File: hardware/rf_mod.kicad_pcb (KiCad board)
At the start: 4 copper layers, 100 x 100 mm, 168 parts, among them J1001 SMA, J1002 SMA, J1003 SMA, J1004 Pmod, J101 SMA, J102 SMA, J103 SMA, J1201 SMA, J1202 SMA, J1301 SMA, J1302 SMA, J1303 SMA, J201 SMA, J202 SMA, J401 SMA, J402 SMA, J501 SMA, J502 SMA, J701 SMA, J702 SMA, J703 SMA, J801 SMA, J802 SMA, J803 SMA, J901 USB-C, J902 SMA, Q1001 AO3401A, Q1201 AO3401A, Q1301 AO3401A, Q501 AO3401A, Q701 AO3401A, Q801 AO3401A, SW1001 ON, SW1201 ON, SW1301 ON, SW501 ON, SW701 ON, SW801 ON, U1001 3.3V, U1002 MAX2871, U101 ADEX-10L+, U1201 GALI-84+, U1301 TRF3722, U1302 3.3V, U501 QPL9547, U701 3.3V, U702 ADL5350, U801 3.3V, U802 ADL5350, U901 MT3608, U902 3.3V, U903 74LVC1G17, X901 25 MHz

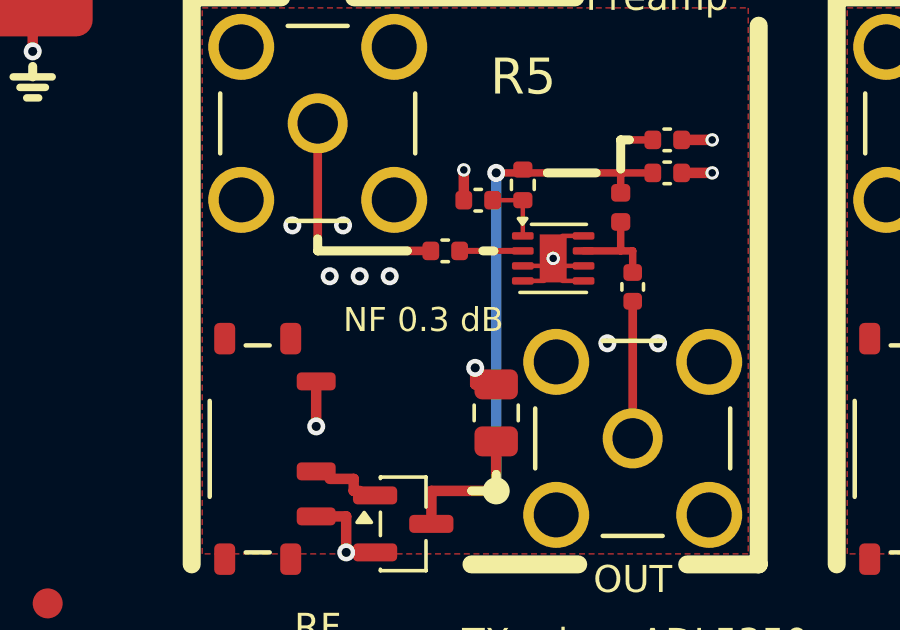
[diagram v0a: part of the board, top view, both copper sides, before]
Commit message: Back-side panels on all six boards; P22 set by hand or by the FPGA; P15 dropped
Jason, Prompt 18: "I hope that the silkscreen (including on the back) is appropriately used to document anything that a
user definitely needs to know to use the tiles successfully and without damaging anything.  If there is additional room
on the back, putting plots of expected responses or other relevant parameters would be great."

- gen_pcb.back_panels: under each tile, mirrored on the back silk, its number and title and the lines in its board's
  BACK dict (levels, loads, supplies, cautions), and where there is one its expected response as a small plot
  (BACK_PLOTS, or the ladder tiles' own simulation; scripts/backplots.py for the rest: amplifiers, datasheet tables,
  the open stub, P23's tuning curve, P10's clipping curve).  A panel goes as one block or in two to four parts, each
  below the one before, clear of the back's tracks and vias where it can be; every panel and plot placed, DRC 0.
- Front silk: Y2 says PULSES ONLY, Y10 "start at mV", R5 and X4 their input level (IN -20 dBm) in place of the noise
  figure.
- P22 (PE43711) on two cells with an 8-way DIP switch: way 1 SPI, ways 2-8 the bits (direct parallel mode with LE pulled
  high), 100 k pull-downs; it still needs the Pmod's 3.3 V.  P15 (two Smith-chart loads) dropped for the cell; P23 moved
  to (3,0).

Co-Authored-By: Claude Opus 5.5 <noreply@anthropic.com>
Claude-Session: https://claude.ai/code/session_01RKeoKvFFzjk3cEBLCXXHnB
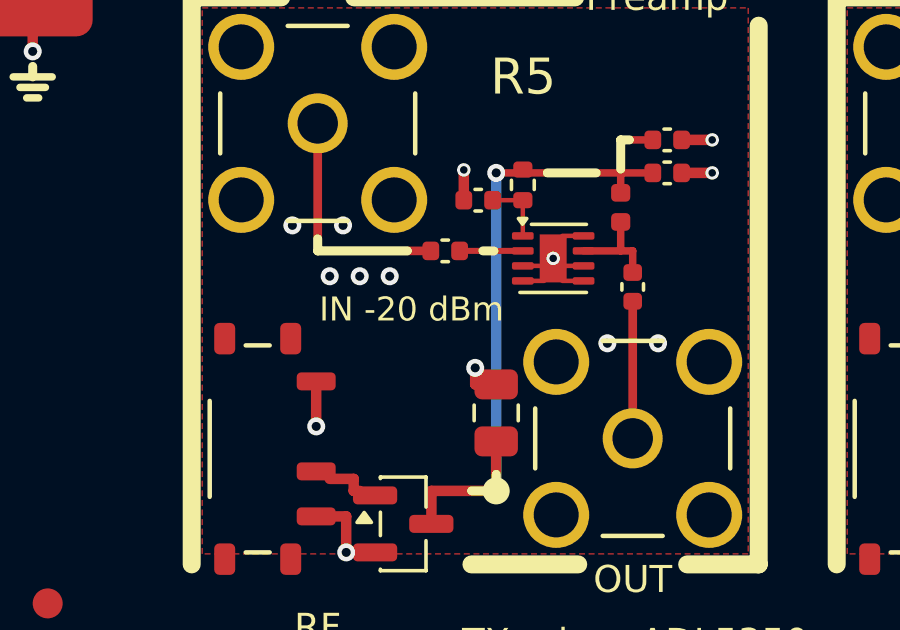
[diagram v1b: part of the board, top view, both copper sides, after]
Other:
- board text added: "+20 dB, OUT"
- board text added: "+22 dBm BURNS"
- board text added: "180 degrees apart"
- board text added: "30 dB pad"
- board text added: "50 ohm"
- board text added: "50 ohm on an unused one"
- board text added: "50 ohm on every port"
- board text added: "I, Q +-1 V into 50 ohm"
- board text added: "IN -20 dBm"
- board text added: "IN < -20 dBm"
- board text added: "IN max +10 dBm"
- board text added: "IN max 0 dBm"
- board text added: "LO 0 to +6 dBm (+4 best)"
- board text added: "OUT A+, A-: -4 to +5 dBm,"
- board text added: "R1 Diode mixer"
- board text added: "R10 Synthesizer"
- board text added: "R12 Gain"
- board text added: "R13 I/Q transmitter"
- board text added: "R2 2.45 GHz filter"
- board text added: "R4 915 MHz filter"
- board text added: "R5 Preamp"
- board text added: "R7 TX mixer ADL5350"
- board text added: "R8 RX mixer ADL5350"
- board text added: "R9 Power"
- board text added: "REF OUT 25 MHz, 1.6 V p-p"
- board text added: "REF: 25 MHz via R10"
- board text added: "RF about -3 dBm"
- board text added: "RF below -5 dBm"
- board text added: "RF, IF max +10 dBm"
- board text added: "USB-C 5 V only"
- board text added: "from a TX"
- board text added: "harmonics below 3 GHz"
- board text added: "image: filter with R2, R4"
- board text added: "into 50 ohm, to R10 REF IN"
- board text added: "max +20 dBm"
- board text added: "slide up: on"
- board text removed: "NF 0.3 dB"

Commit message: One letter per board, tiles in lower case: AMOD-P2 is AMOD-N (n1-n11), RF-MOD-2 is IQ-MOD (q1-q11), PhMOD's tiles h1-h10
Jason, Prompt 19: "If we can have a nice, well justified single-letter designator for each board, it would make
everything much more clear", and "d11, q11, and c11 don't look like obvious electronics or PCB things".

- p passive, n networks (AMOD-P2's P14, P16-P25), a active, r radio, h PhMOD (Y1-Y10), q quadrature (RF-MOD-2's X1-X11);
  c, m and b are taken for the conversion, motor and brushless boards to come.  PLAN.md section 13 has the table and
  the reasons (no letter moves to another board, no retired name is reused, no s: s11 is the reflection coefficient).
- Every tile name in lower case on the silk, in the code (Tile ids, BACK/BACK_PLOTS/DOCS keys, the nets built on them),
  the handbooks, README, DOA lists, KIT, PLAN and the review brief; pin names (USB-C A1...), the 4046's R1/C1, nets
  named N1/P1, part numbers ending -R7 and the paper size A1 left alone.  tiles.dump refuses a tile not named
  <letter><n>, a number twice, and a BACK key for a tile that does not exist.
- Board and file renames: boards/amod_n.py, boards/iq_mod.py, docs/DOA_amod_n.md, docs/DOA_iq_mod.md, the handbooks,
  the generated hardware, outputs and pictures.  Silk nudged where a lower-case p or q hung onto the line below.
- All six boards rebuilt: ERC 0, DRC 0, every check.

Co-Authored-By: Claude Opus 5.5 <noreply@anthropic.com>
Claude-Session: https://claude.ai/code/session_01RKeoKvFFzjk3cEBLCXXHnB
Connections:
- net /R10_AN renamed /r10_AN
- net /R10_AP renamed /r10_AP
- net /R10_BF renamed /r10_BF
- net /R10_CP renamed /r10_CP
- net /R10_G renamed /r10_G
- net /R10_LD renamed /r10_LD
- net /R10_LEDA renamed /r10_LEDA
- net /R10_N2 renamed /r10_N2
- net /R10_NF renamed /r10_NF
- net /R10_OUTA renamed /r10_OUTA
- net /R10_OUTAN renamed /r10_OUTAN
- net /R10_REFI renamed /r10_REFI
- net /R10_REG renamed /r10_REG
- net /R10_RS renamed /r10_RS
- net /R10_TN renamed /r10_TN
- net /R10_V33 renamed /r10_V33
- net /R10_VS renamed /r10_VS
- net /R12_G renamed /r12_G
- net /R12_IN renamed /r12_IN
- net /R12_IN_A renamed /r12_IN_A
- net /R12_OUT renamed /r12_OUT
- net /R12_OUT_A renamed /r12_OUT_A
- net /R12_VD renamed /r12_VD
- net /R12_VS renamed /r12_VS
- net /R13_BBI renamed /r13_BBI
- net /R13_BBQ renamed /r13_BBQ
- net /R13_BIN renamed /r13_BIN
- net /R13_BIP renamed /r13_BIP
- net /R13_BQN renamed /r13_BQN
- net /R13_BQP renamed /r13_BQP
- net /R13_CP renamed /r13_CP
- net /R13_G renamed /r13_G
- net /R13_LD renamed /r13_LD
- net /R13_LEDA renamed /r13_LEDA
- net /R13_N2 renamed /r13_N2
- net /R13_REFI renamed /r13_REFI
- net /R13_RFO renamed /r13_RFO
- net /R13_RFOUT renamed /r13_RFOUT
- net /R13_V33 renamed /r13_V33
- net /R13_VS renamed /r13_VS
- net /R13_VT renamed /r13_VT
- net /R1_IF renamed /r1_IF
- net /R1_LO renamed /r1_LO
- net /R1_RF renamed /r1_RF
- net /R2_IN renamed /r2_IN
- net /R2_OUT renamed /r2_OUT
- net /R4_IN renamed /r4_IN
- net /R4_OUT renamed /r4_OUT
- net /R5_G renamed /r5_G
- net /R5_IN renamed /r5_IN
- net /R5_IN_A renamed /r5_IN_A
- net /R5_OUT renamed /r5_OUT
- net /R5_OUT_A renamed /r5_OUT_A
- net /R5_VB renamed /r5_VB
- net /R5_VS renamed /r5_VS
- net /R7_G renamed /r7_G
- net /R7_IF renamed /r7_IF
- net /R7_IFN renamed /r7_IFN
- net /R7_LOC renamed /r7_LOC
- net /R7_LOJ renamed /r7_LOJ
- net /R7_LON renamed /r7_LON
- net /R7_RFIF renamed /r7_RFIF
- net /R7_RFN renamed /r7_RFN
- net /R7_V33 renamed /r7_V33
- net /R7_VPOS renamed /r7_VPOS
- net /R7_VS renamed /r7_VS
- net /R8_G renamed /r8_G
- net /R8_IF renamed /r8_IF
- net /R8_IFN renamed /r8_IFN
- net /R8_LOC renamed /r8_LOC
- net /R8_LOJ renamed /r8_LOJ
- net /R8_LON renamed /r8_LON
- net /R8_RFIF renamed /r8_RFIF
- net /R8_RFN renamed /r8_RFN
- net /R8_V33 renamed /r8_V33
- net /R8_VPOS renamed /r8_VPOS
- net /R8_VS renamed /r8_VS
- net /R9_BUF renamed /r9_BUF
- net /R9_CC1 renamed /r9_CC1
- net /R9_CC2 renamed /r9_CC2
- net /R9_FB renamed /r9_FB
- net /R9_LEDG renamed /r9_LEDG
- net /R9_LEDY renamed /r9_LEDY
- net /R9_OSC renamed /r9_OSC
- net /R9_REF renamed /r9_REF
- net /R9_SW renamed /r9_SW
- net /R9_VBUS renamed /r9_VBUS
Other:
- board text added: "REF: 25 MHz via r10"
- board text added: "image: filter with r2, r4"
- board text added: "into 50 ohm, to r10 REF IN"
- board text added: "r1"
- board text added: "r1 Diode mixer"
- board text added: "r10"
- board text added: "r10 Synthesizer"
- board text added: "r12"
- board text added: "r12 Gain"
- board text added: "r13"
- board text added: "r13 I/Q transmitter"
- board text added: "r2"
- board text added: "r2 2.45 GHz filter"
- board text added: "r4"
- board text added: "r4 915 MHz filter"
- board text added: "r5"
- board text added: "r5 Preamp"
- board text added: "r7"
- board text added: "r7 TX mixer ADL5350"
- board text added: "r8"
- board text added: "r8 RX mixer ADL5350"
- board text added: "r9"
- board text added: "r9 Power"
- board text added: "switch (up: on). Power: USB-C on r9. The handbook has"
- board text removed: "R1"
- board text removed: "R1 Diode mixer"
- board text removed: "R10"
- board text removed: "R10 Synthesizer"
- board text removed: "R12"
- board text removed: "R12 Gain"
- board text removed: "R13"
- board text removed: "R13 I/Q transmitter"
- board text removed: "R2"
- board text removed: "R2 2.45 GHz filter"
- board text removed: "R4"
- board text removed: "R4 915 MHz filter"
- board text removed: "R5"
- board text removed: "R5 Preamp"
- board text removed: "R7"
- board text removed: "R7 TX mixer ADL5350"
- board text removed: "R8"
- board text removed: "R8 RX mixer ADL5350"
- board text removed: "R9"
- board text removed: "R9 Power"
- board text removed: "REF: 25 MHz via R10"
- board text removed: "image: filter with R2, R4"
- board text removed: "into 50 ohm, to R10 REF IN"
- board text removed: "switch (up: on). Power: USB-C on R9. The handbook has"

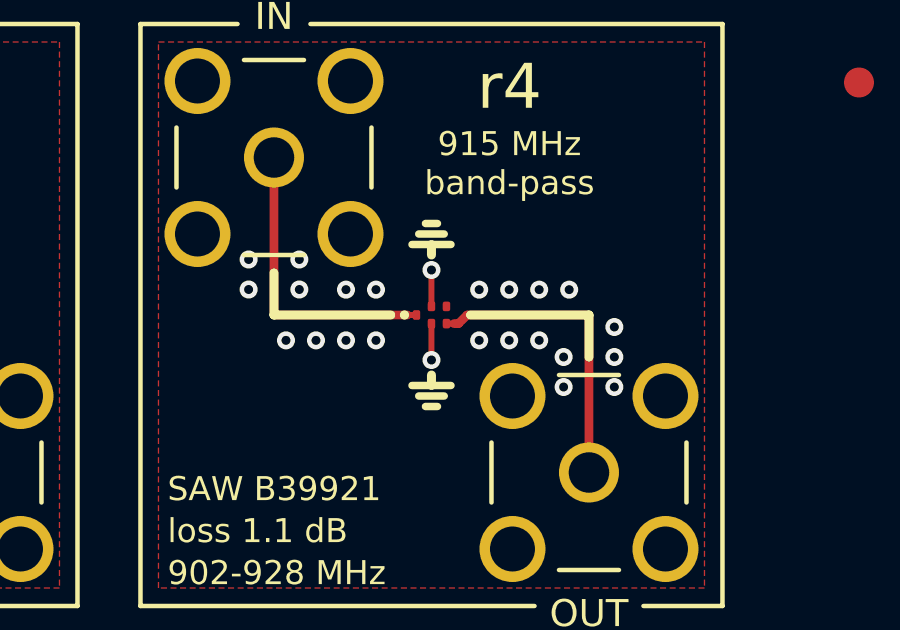
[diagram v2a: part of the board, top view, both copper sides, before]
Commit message: Two pinouts read against their datasheets and fixed: the DMMT3904W (AMOD-C's c9 and c10) is 1 B2, 2 B1, 3 C1, 4 E1, 5 E2, 6 C2, not the BCM857BS's order (c9's pair turned 180 with IN+ under it on the back, c10's turned 180 with Q1's base on the back); RF-MOD's 915 MHz SAW has its output on pad 4, not 3 (r4 took it from a ground pad). scripts/check_pinouts.py compares every symbol's pin names with EasyEDA's: these two were its only real disagreements
Co-Authored-By: Claude Opus 5.5 <noreply@anthropic.com>
Claude-Session: https://claude.ai/code/session_01RKeoKvFFzjk3cEBLCXXHnB
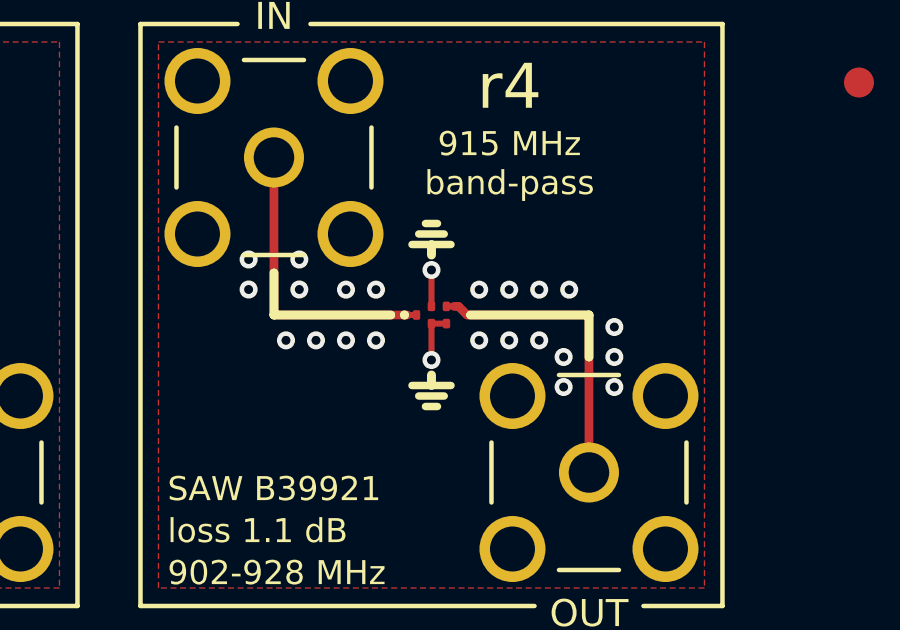
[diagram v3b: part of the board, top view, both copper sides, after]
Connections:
- FL401 pad 3: /r4_OUT -> GND
- FL401 pad 4: GND -> /r4_OUT
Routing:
- net GND: track 154.2 -> 154.7 mm
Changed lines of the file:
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@@
 			(layers "F.Cu" "F.Mask" "F.Paste")
 			(roundrect_rratio 0.25)
-			(net "/r4_OUT")
+			(net "GND")
 		)
 		(pad "4" smd roundrect
@@
 			(layers "F.Cu" "F.Mask" "F.Paste")
 			(roundrect_rratio 0.25)
-			(net "GND")
+			(net "/r4_OUT")
 		)
 		(pad "5" smd roundrect
@@
 	)
 	(segment
+		(start 28.75 12.5)
+		(end 34 12.5)
+		(width 0.29)
+		(layer "F.Cu")
+		(net "/r1_RF")
+	)
+	(segment
 		(start 25.54 15.789)
 		(end 27.15 15.79)
@@
 	)
 	(segment
-		(start 28.75 12.5)
-		(end 34 12.5)
+		(start 55.5 12.5)
+		(end 55.5 17.75)
 		(width 0.29)
 		(layer "F.Cu")
-		(net "/r1_RF")
+		(net "/r2_IN")
 	)
 	(segment
@@
 	)
 	(segment
-		(start 55.5 12.5)
-		(end 55.5 17.75)
+		(start 61.65 17.75)
+		(end 66 17.75)
 		(width 0.29)
 		(layer "F.Cu")
-		(net "/r2_IN")
+		(net "/r2_OUT")
 	)
 	(segment
@@
 	)
 	(segment
-		(start 61.65 17.75)
-		(end 66 17.75)
-		(width 0.29)
+		(start 81.45 17.75)
+		(end 81.75 17.75)
+		(width 0.2)
 		(layer "F.Cu")
-		(net "/r2_OUT")
+		(net "/r4_IN")
 	)
 	(segment
@@
 	)
 	(segment
-		(start 81.45 17.75)
-		(end 81.75 17.75)
-		(width 0.2)
-		(layer "F.Cu")
-		(net "/r4_IN")
-	)
-	(segment
 		(start 77 12.5)
 		(end 77 17.75)
@@
 	)
 	(segment
-		(start 83.15 18.037)
-		(end 83.44 17.75)
+		(start 83.44 17.75)
+		(end 87.5 17.75)
 		(width 0.29)
 		(layer "F.Cu")
@@
 	)
 	(segment
-		(start 83 18.037)
-		(end 83.15 18.037)
-		(width 0.29)
+		(start 82.75 17.463)
+		(end 83 17.463)
+		(width 0.2)
 		(layer "F.Cu")
 		(net "/r4_OUT")
 	)
 	(segment
-		(start 87.5 17.75)
-		(end 87.5 23)
+		(start 83 17.463)
+		(end 83.15 17.463)
 		(width 0.29)
 		(layer "F.Cu")
@@
 	)
 	(segment
-		(start 82.75 18.037)
-		(end 83 18.037)
-		(width 0.2)
+		(start 87.5 17.75)
+		(end 87.5 23)
+		(width 0.29)
 		(layer "F.Cu")
 		(net "/r4_OUT")
 	)
 	(segment
-		(start 83.44 17.75)
-		(end 87.5 17.75)
+		(start 83.15 17.463)
+		(end 83.44 17.75)
 		(width 0.29)
 		(layer "F.Cu")
@@
 	)
 	(segment
-		(start 25.54 10.711)
-		(end 25.54 8.7)
-		(width 0.29)
-		(layer "F.Cu")
-		(net "GND")
-	)
-	(segment
 		(start 67.5875 84.45)
 		(end 66.45 84.45)
@@
 	)
 	(segment
-		(start 20.46 15.789)
-		(end 18.65 15.79)
-		(width 0.29)
-		(layer "F.Cu")
-		(net "GND")
-	)
-	(segment
 		(start 93.505 42.5)
 		(end 94.419999 43.57)
@@
 	)
 	(segment
+		(start 25.54 10.711)
+		(end 25.54 8.7)
+		(width 0.29)
+		(layer "F.Cu")
+		(net "GND")
+	)
+	(segment
 		(start 20.001 59.848)
 		(end 19.999 60.75)
@@
 	)
 	(segment
+		(start 23 10.711)
+		(end 23 8.7)
+		(width 0.29)
+		(layer "F.Cu")
+		(net "GND")
+	)
+	(segment
 		(start 36.2 83.15)
 		(end 36.2 82.05)
@@
 	)
 	(segment
+		(start 60.75 17.176)
+		(end 60.75 16.149999)
+		(width 0.29)
+		(layer "F.Cu")
+		(net "GND")
+	)
+	(segment
 		(start 20.75 89.925)
 		(end 20.75 90.65)
@@
 	)
 	(segment
+		(start 82.75 18.037)
+		(end 82.25 18.037)
+		(width 0.2)
+		(layer "F.Cu")
+		(net "GND")
+	)
+	(segment
 		(start 58.95 62.635)
 		(end 58.95 63.45)
@@
 	)
 	(segment
+		(start 60.75 18.324)
+		(end 60.75 19.35)
+		(width 0.29)
+		(layer "F.Cu")
+		(net "GND")
+	)
+	(segment
 		(start 32.45 64.099999)
 		(end 32.45 65.599999)
@@
 	)
 	(segment
-		(start 23 10.711)
-		(end 23 8.7)
-		(width 0.29)
-		(layer "F.Cu")
-		(net "GND")
-	)
-	(segment
 		(start 62.85 66.23)
 		(end 62.85 67.15)
@@
 	)
 	(segment
-		(start 60.75 18.324)
-		(end 60.75 19.35)
-		(width 0.29)
-		(layer "F.Cu")
-		(net "GND")
-	)
-	(segment
 		(start 39.95 42.7)
 		(end 39.25 42.7)
@@
 	)
 	(segment
+		(start 20.46 15.789)
+		(end 18.65 15.79)
+		(width 0.29)
+		(layer "F.Cu")
+		(net "GND")
+	)
+	(segment
 		(start 66.4 86.1375)
 		(end 66.4 85.15)
@@
 	)
 	(segment
-		(start 60.75 17.176)
-		(end 60.75 16.149999)
-		(width 0.29)
-		(layer "F.Cu")
-		(net "GND")
-	)
-	(segment
 		(start 21.5 85.1875)
 		(end 21.5 84.05)
@@
 	)
 	(via
-		(at 18.65 15.79)
-		(size 0.6)
-		(drill 0.3)
-		(layers "F.Cu" "B.Cu")
-		(tenting
-			(front yes)
-			(back yes)
-		)
-		(net "GND")
-	)
-	(via
 		(at 63.05 16.905)
 		(size 0.6)
@@
 	)
 	(via
+		(at 60.75 16.149999)
+		(size 0.6)
+		(drill 0.3)
+		(layers "F.Cu" "B.Cu")
+		(tenting
+			(front yes)
+			(back yes)
+		)
+		(net "GND")
+	)
+	(via
 		(at 15.405 88.43)
 		(size 0.6)
@@
 	)
 	(via
-		(at 60.75 16.149999)
-		(size 0.6)
-		(drill 0.3)
-		(layers "F.Cu" "B.Cu")
-		(tenting
-			(front yes)
-			(back yes)
-		)
-		(net "GND")
-	)
-	(via
 		(at 15.405 91.43)
 		(size 0.6)
@@
 	)
 	(via
+		(at 18.65 15.79)
+		(size 0.6)
+		(drill 0.3)
+		(layers "F.Cu" "B.Cu")
+		(tenting
+			(front yes)
+			(back yes)
+		)
+		(net "GND")
+	)
+	(via
 		(at 60.67 73.2)
 		(size 0.45)
@@
 	)
 	(via
+		(at 25.54 8.7)
+		(size 0.6)
+		(drill 0.3)
+		(layers "F.Cu" "B.Cu")
+		(tenting
+			(front yes)
+			(back yes)
+		)
+		(net "GND")
+	)
+	(via
 		(at 41.05 61.35)
 		(size 0.6)
@@
 	)
 	(via
-		(at 79.2 60.55)
+		(at 23 8.7)
 		(size 0.6)
 		(drill 0.3)
@@
 	)
 	(via
-		(at 60.75 19.35)
+		(at 79.2 60.55)
 		(size 0.6)
 		(drill 0.3)
@@
 	)
 	(via
-		(at 27.65 94.345)
+		(at 60.75 19.35)
 		(size 0.6)
 		(drill 0.3)
@@
 	)
 	(via
-		(at 21.85 82.15)
+		(at 27.65 94.345)
 		(size 0.6)
 		(drill 0.3)
@@
 	)
 	(via
-		(at 54.655 58.9)
+		(at 21.85 82.15)
 		(size 0.6)
 		(drill 0.3)
@@
 	)
 	(via
-		(at 37.58 40.595)
+		(at 54.655 58.9)
 		(size 0.6)
 		(drill 0.3)
@@
 	)
 	(via
-		(at 76.23 82.105)
+		(at 37.58 40.595)
 		(size 0.6)
 		(drill 0.3)
@@
 	)
 	(via
-		(at 43.885 41.15)
+		(at 76.23 82.105)
 		(size 0.6)
 		(drill 0.3)
@@
 	)
 	(via
-		(at 78.85 64.75)
+		(at 43.885 41.15)
 		(size 0.6)
 		(drill 0.3)
@@
 	)
 	(via
-		(at 23 8.7)
+		(at 78.85 64.75)
 		(size 0.6)
 		(drill 0.3)
@@
 		(size 0.6)
 		(drill 0.3)
-		(layers "F.Cu" "B.Cu")
-		(tenting
-			(front yes)
-			(back yes)
-		)
-		(net "GND")
-	)
-	(via
-		(at 25.54 8.7)
-		(size 0.6)
-		(drill 0.3)
